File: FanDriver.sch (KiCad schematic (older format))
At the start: 0 parts

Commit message: updated fan control seyion
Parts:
- added Q?: MOSFET_N, symbol MOSFET_N
- added R?: R, symbol R
- added RV?: POT, symbol POT
- added U?: LM324, symbol LM324
- added U?: ADC0832, symbol ADC0832
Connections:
- net labels added: +12V, -12V, GND
- wire segments 0 -> 17
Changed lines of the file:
@@
-EESchema Schematic File Version 2  date Wed 05 Feb 2014 12:50:12 AM EST
+EESchema Schematic File Version 2  date Thu 06 Feb 2014 12:03:54 AM EST
 LIBS:power
 LIBS:device
@@
 Sheet 4 8
 Title ""
-Date "5 feb 2014"
+Date "6 feb 2014"
 Rev ""
 Comp ""
@@
 Comment4 ""
 $EndDescr
-Text HLabel 3300 1900 0    60   Input ~ 0
+$Comp
+L ADC0832 U?
+U 1 1 52F316A2
+P 3550 2150
+F 0 "U?" H 3550 2250 70  0000 C CNN
+F 1 "ADC0832" H 3550 2051 70  0000 C CNN
+	1    3550 2150
+	1    0    0    -1
+$EndComp
+Wire Wire Line
+	5100 3000 5100 3450
+Wire Wire Line
+	5100 2300 6650 2300
+Wire Wire Line
+	7050 1750 7050 2000
+Connection ~ 8400 2900
+Wire Wire Line
+	8400 2900 6400 2900
+Wire Wire Line
+	6400 2900 6400 2500
+Wire Wire Line
+	6400 2500 6650 2500
+Wire Wire Line
+	8400 1800 8400 2200
+Wire Wire Line
+	7650 2400 8100 2400
+Wire Wire Line
+	8400 2600 8400 2950
+Wire Wire Line
+	8400 2950 10850 2950
+Wire Wire Line
+	10850 3150 8450 3150
+Wire Wire Line
+	8450 3150 8450 3450
+Wire Wire Line
+	7050 2800 7050 2850
+Wire Wire Line
+	7050 2850 7300 2850
+Wire Wire Line
+	7300 2850 7300 2800
+Wire Wire Line
+	5100 1450 5100 1650
+Wire Wire Line
+	5100 2500 5100 2150
+Connection ~ 5100 2300
+$Comp
+L GND #PWR?
+U 1 1 52F31662
+P 5100 3450
+F 0 "#PWR?" H 5100 3450 30  0001 C CNN
+F 1 "GND" H 5100 3380 30  0001 C CNN
+	1    5100 3450
+	1    0    0    -1
+$EndComp
+$Comp
+L R R?
+U 1 1 52F31643
+P 5100 1900
+F 0 "R?" V 5180 1900 50  0000 C CNN
+F 1 "R" V 5100 1900 50  0000 C CNN
+	1    5100 1900
+	1    0    0    -1
+$EndComp
+$Comp
+L POT RV?
+U 1 1 52F315F5
+P 5100 2750
+F 0 "RV?" H 5100 2650 50  0000 C CNN
+F 1 "POT" H 5100 2750 50  0000 C CNN
+	1    5100 2750
+	0    -1   1    0
+$EndComp
+$Comp
+L +12V #PWR?
+U 1 1 52F315D4
+P 5100 1450
+F 0 "#PWR?" H 5100 1400 20  0001 C CNN
+F 1 "+12V" H 5100 1550 30  0000 C CNN
+	1    5100 1450
+	1    0    0    -1
+$EndComp
+$Comp
+L -12V #PWR?
+U 1 1 52F31549
+P 7300 2800
+F 0 "#PWR?" H 7300 2930 20  0001 C CNN
+F 1 "-12V" H 7300 2900 30  0000 C CNN
+	1    7300 2800
+	1    0    0    -1
+$EndComp
+$Comp
+L +12V #PWR?
+U 1 1 52F31538
+P 7050 1750
+F 0 "#PWR?" H 7050 1700 20  0001 C CNN
+F 1 "+12V" H 7050 1850 30  0000 C CNN
+	1    7050 1750
+	1    0    0    -1
+$EndComp
+$Comp
+L GND #PWR?
+U 1 1 52F313E3
+P 8450 3450
+F 0 "#PWR?" H 8450 3450 30  0001 C CNN
+F 1 "GND" H 8450 3380 30  0001 C CNN
+	1    8450 3450
+	1    0    0    -1
+$EndComp
+$Comp
+L +12V #PWR?
+U 1 1 52F31370
+P 8400 1800
+F 0 "#PWR?" H 8400 1750 20  0001 C CNN
+F 1 "+12V" H 8400 1900 30  0000 C CNN
+	1    8400 1800
+	1    0    0    -1
+$EndComp
+$Comp
+L MOSFET_N Q?
+U 1 1 52F31276
+P 8300 2400
+F 0 "Q?" H 8310 2570 60  0000 R CNN
+F 1 "MOSFET_N" H 8310 2250 60  0000 R CNN
+	1    8300 2400
+	1    0    0    -1
+$EndComp
+$Comp
+L LM324 U?
+U 1 1 52F311E8
+P 7150 2400
+F 0 "U?" H 7200 2600 60  0000 C CNN
+F 1 "LM324" H 7300 2200 50  0000 C CNN
+	1    7150 2400
+	1    0    0    -1
+$EndComp
+Text HLabel 1650 2400 0    60   Input ~ 0
 FanIn
-Text HLabel 3300 1750 0    60   Output ~ 0
+Text HLabel 1650 2250 0    60   Output ~ 0
 TacOut
-Text HLabel 8250 2750 0    60   Input ~ 0
+Text HLabel 10850 3450 0    60   Input ~ 0
 TacIn
-Text HLabel 8250 2450 0    60   Input ~ 0
+Text HLabel 10850 3150 0    60   Input ~ 0
 PWR-
-Text HLabel 8250 2250 0    60   Output ~ 0
+Text HLabel 10850 2950 0    60   Output ~ 0
 PWR+
 $EndSCHEMATC

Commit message: Updated with correct DAC and ADC for thermo and fan
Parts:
- removed U?: ADC0832, symbol ADC0832
- added R? (x4): R, symbol R
- added U?: MCP4921-E/SN, SO8, symbol MCP4921-E/SN
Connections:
- net labels added: CS_N, CurrentMeasure, MISO, MOSI, S_CLK
- wire segments 17 -> 30
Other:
- moved on the sheet: RV?
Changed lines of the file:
@@
-EESchema Schematic File Version 2  date Thu 06 Feb 2014 12:03:54 AM EST
+EESchema Schematic File Version 2
 LIBS:power
 LIBS:device
@@
 LIBS:valves
 LIBS:InitialKiCadProject-cache
-EELAYER 25  0
+EELAYER 27 0
 EELAYER END
-$Descr A4 11700 8267
+$Descr A4 11693 8268
 encoding utf-8
 Sheet 4 8
 Title ""
-Date "6 feb 2014"
+Date "7 feb 2014"
 Rev ""
 Comp ""
@@
 $EndDescr
 $Comp
-L ADC0832 U?
-U 1 1 52F316A2
-P 3550 2150
-F 0 "U?" H 3550 2250 70  0000 C CNN
-F 1 "ADC0832" H 3550 2051 70  0000 C CNN
-	1    3550 2150
-	1    0    0    -1
-$EndComp
-Wire Wire Line
-	5100 3000 5100 3450
-Wire Wire Line
-	5100 2300 6650 2300
-Wire Wire Line
-	7050 1750 7050 2000
-Connection ~ 8400 2900
-Wire Wire Line
-	8400 2900 6400 2900
-Wire Wire Line
-	6400 2900 6400 2500
-Wire Wire Line
-	6400 2500 6650 2500
-Wire Wire Line
-	8400 1800 8400 2200
-Wire Wire Line
-	7650 2400 8100 2400
-Wire Wire Line
-	8400 2600 8400 2950
-Wire Wire Line
-	8400 2950 10850 2950
-Wire Wire Line
-	10850 3150 8450 3150
-Wire Wire Line
-	8450 3150 8450 3450
-Wire Wire Line
-	7050 2800 7050 2850
-Wire Wire Line
-	7050 2850 7300 2850
-Wire Wire Line
-	7300 2850 7300 2800
-Wire Wire Line
-	5100 1450 5100 1650
-Wire Wire Line
-	5100 2500 5100 2150
-Connection ~ 5100 2300
-$Comp
 L GND #PWR?
 U 1 1 52F31662
-P 5100 3450
-F 0 "#PWR?" H 5100 3450 30  0001 C CNN
-F 1 "GND" H 5100 3380 30  0001 C CNN
-	1    5100 3450
+P 4800 3000
+F 0 "#PWR?" H 4800 3000 30  0001 C CNN
+F 1 "GND" H 4800 2930 30  0001 C CNN
+F 2 "" H 4800 3000 60  0001 C CNN
+F 3 "" H 4800 3000 60  0001 C CNN
+	1    4800 3000
 	1    0    0    -1
 $EndComp
@@
 F 0 "R?" V 5180 1900 50  0000 C CNN
 F 1 "R" V 5100 1900 50  0000 C CNN
+F 2 "" H 5100 1900 60  0001 C CNN
+F 3 "" H 5100 1900 60  0001 C CNN
 	1    5100 1900
 	1    0    0    -1
@@
 L POT RV?
 U 1 1 52F315F5
-P 5100 2750
-F 0 "RV?" H 5100 2650 50  0000 C CNN
-F 1 "POT" H 5100 2750 50  0000 C CNN
-	1    5100 2750
+P 5100 2650
+F 0 "RV?" H 5100 2550 50  0000 C CNN
+F 1 "POT" H 5100 2650 50  0000 C CNN
+F 2 "" H 5100 2650 60  0001 C CNN
+F 3 "" H 5100 2650 60  0001 C CNN
+	1    5100 2650
 	0    -1   1    0
 $EndComp
@@
 F 0 "#PWR?" H 5100 1400 20  0001 C CNN
 F 1 "+12V" H 5100 1550 30  0000 C CNN
+F 2 "" H 5100 1450 60  0001 C CNN
+F 3 "" H 5100 1450 60  0001 C CNN
 	1    5100 1450
 	1    0    0    -1
@@
 F 0 "#PWR?" H 7300 2930 20  0001 C CNN
 F 1 "-12V" H 7300 2900 30  0000 C CNN
+F 2 "" H 7300 2800 60  0001 C CNN
+F 3 "" H 7300 2800 60  0001 C CNN
 	1    7300 2800
 	1    0    0    -1
@@
 F 0 "#PWR?" H 7050 1700 20  0001 C CNN
 F 1 "+12V" H 7050 1850 30  0000 C CNN
+F 2 "" H 7050 1750 60  0001 C CNN
+F 3 "" H 7050 1750 60  0001 C CNN
 	1    7050 1750
 	1    0    0    -1
@@
 L GND #PWR?
 U 1 1 52F313E3
-P 8450 3450
-F 0 "#PWR?" H 8450 3450 30  0001 C CNN
-F 1 "GND" H 8450 3380 30  0001 C CNN
-	1    8450 3450
+P 7600 4450
+F 0 "#PWR?" H 7600 4450 30  0001 C CNN
+F 1 "GND" H 7600 4380 30  0001 C CNN
+F 2 "" H 7600 4450 60  0001 C CNN
+F 3 "" H 7600 4450 60  0001 C CNN
+	1    7600 4450
 	1    0    0    -1
 $EndComp
@@
 F 0 "#PWR?" H 8400 1750 20  0001 C CNN
 F 1 "+12V" H 8400 1900 30  0000 C CNN
+F 2 "" H 8400 1800 60  0001 C CNN
+F 3 "" H 8400 1800 60  0001 C CNN
 	1    8400 1800
 	1    0    0    -1
@@
 F 0 "Q?" H 8310 2570 60  0000 R CNN
 F 1 "MOSFET_N" H 8310 2250 60  0000 R CNN
+F 2 "" H 8300 2400 60  0001 C CNN
+F 3 "" H 8300 2400 60  0001 C CNN
 	1    8300 2400
 	1    0    0    -1
@@
 F 0 "U?" H 7200 2600 60  0000 C CNN
 F 1 "LM324" H 7300 2200 50  0000 C CNN
+F 2 "" H 7150 2400 60  0001 C CNN
+F 3 "" H 7150 2400 60  0001 C CNN
 	1    7150 2400
 	1    0    0    -1
 $EndComp
-Text HLabel 1650 2400 0    60   Input ~ 0
+Text HLabel 1950 3200 0    60   Input ~ 0
 FanIn
-Text HLabel 1650 2250 0    60   Output ~ 0
+Text HLabel 1650 5050 0    60   Output ~ 0
 TacOut
-Text HLabel 10850 3450 0    60   Input ~ 0
+Text HLabel 10700 5050 0    60   Input ~ 0
 TacIn
-Text HLabel 10850 3150 0    60   Input ~ 0
+Text HLabel 10900 3300 0    60   Input ~ 0
 PWR-
 Text HLabel 10850 2950 0    60   Output ~ 0
 PWR+
+Text HLabel 1950 3300 0    60   Output ~ 0
+CurrentMeasure
+$Comp
+L R R?
+U 1 1 52F43F3A
+P 7600 4000
+F 0 "R?" V 7680 4000 50  0000 C CNN
+F 1 "R" V 7600 4000 50  0000 C CNN
+F 2 "" H 7600 4000 60  0001 C CNN
+F 3 "" H 7600 4000 60  0001 C CNN
+	1    7600 4000
+	1    0    0    -1
+$EndComp
+Connection ~ 7600 3300
+Wire Wire Line
+	7600 4250 7600 4450
+Wire Wire Line
+	6600 2500 6650 2500
+Wire Wire Line
+	6600 3300 6600 2500
+Wire Wire Line
+	1950 3300 10900 3300
+Wire Wire Line
+	7600 3750 7600 3300
+Wire Wire Line
+	10700 5050 1650 5050
+Connection ~ 5100 2300
+Wire Wire Line
+	5100 2150 5100 2400
+Wire Wire Line
+	5100 1450 5100 1650
+Wire Wire Line
+	7300 2850 7300 2800
+Wire Wire Line
+	7050 2850 7300 2850
+Wire Wire Line
+	7050 2800 7050 2850
+Wire Wire Line
+	8400 2950 10850 2950
+Wire Wire Line
+	8400 2600 8400 2950
+Wire Wire Line
+	7650 2400 8100 2400
+Wire Wire Line
+	8400 1800 8400 2200
+Connection ~ 8400 2900
+Wire Wire Line
+	7050 1750 7050 2000
+Wire Wire Line
+	5100 2300 6650 2300
+Connection ~ 6600 3300
+$Comp
+L R R?
+U 1 1 52F4401D
+P 4300 2200
+F 0 "R?" V 4380 2200 50  0000 C CNN
+F 1 "R" V 4300 2200 50  0000 C CNN
+F 2 "" H 4300 2200 60  0001 C CNN
+F 3 "" H 4300 2200 60  0001 C CNN
+	1    4300 2200
+	0    -1   -1   0
+$EndComp
+Wire Wire Line
+	3700 2200 4050 2200
+Wire Wire Line
+	4550 2200 5100 2200
+Connection ~ 5100 2200
+$Comp
+L R R?
+U 1 1 52F44054
+P 6000 2850
+F 0 "R?" V 6080 2850 50  0000 C CNN
+F 1 "R" V 6000 2850 50  0000 C CNN
+F 2 "" H 6000 2850 60  0001 C CNN
+F 3 "" H 6000 2850 60  0001 C CNN
+	1    6000 2850
+	1    0    0    -1
+$EndComp
+Wire Wire Line
+	6000 2600 6000 2300
+Connection ~ 6000 2300
+Wire Wire Line
+	6000 3100 6000 3200
+Wire Wire Line
+	6000 3200 1950 3200
+Text HLabel 2050 1800 0    60   Output ~ 0
+MISO
+Text HLabel 2100 2050 0    60   Input ~ 0
+MOSI
+Text HLabel 2100 2250 0    60   Input ~ 0
+CS_N
+Text HLabel 2100 2150 0    60   Input ~ 0
+S_CLK
+$Comp
+L MCP4921-E/SN U?
+U 1 1 52F441DE
+P 3150 2200
+F 0 "U?" H 3150 2550 40  0000 L BNN
+F 1 "MCP4921-E/SN" H 3150 2500 40  0000 L BNN
+F 2 "SO8" H 3150 2200 30  0000 C CIN
+F 3 "" H 3150 2200 60  0000 C CNN
+	1    3150 2200
+	1    0    0    -1
+$EndComp
+Wire Wire Line
+	2100 2050 2600 2050
+Wire Wire Line
+	2100 2150 2600 2150
+Wire Wire Line
+	2100 2250 2600 2250
+$Comp
+L R R?
+U 1 1 52F44272
+P 2350 2750
+F 0 "R?" V 2430 2750 50  0000 C CNN
+F 1 "R" V 2350 2750 50  0000 C CNN
+F 2 "" H 2350 2750 60  0001 C CNN
+F 3 "" H 2350 2750 60  0001 C CNN
+	1    2350 2750
+	1    0    0    -1
+$EndComp
+Wire Wire Line
+	2350 2500 2350 2350
+Wire Wire Line
+	2350 2350 2600 2350
+Wire Wire Line
+	2350 3000 2350 3200
+Connection ~ 2350 3200
+Wire Wire Line
+	4950 2650 4800 2650
+Wire Wire Line
+	4800 2650 4800 3000
 $EndSCHEMATC

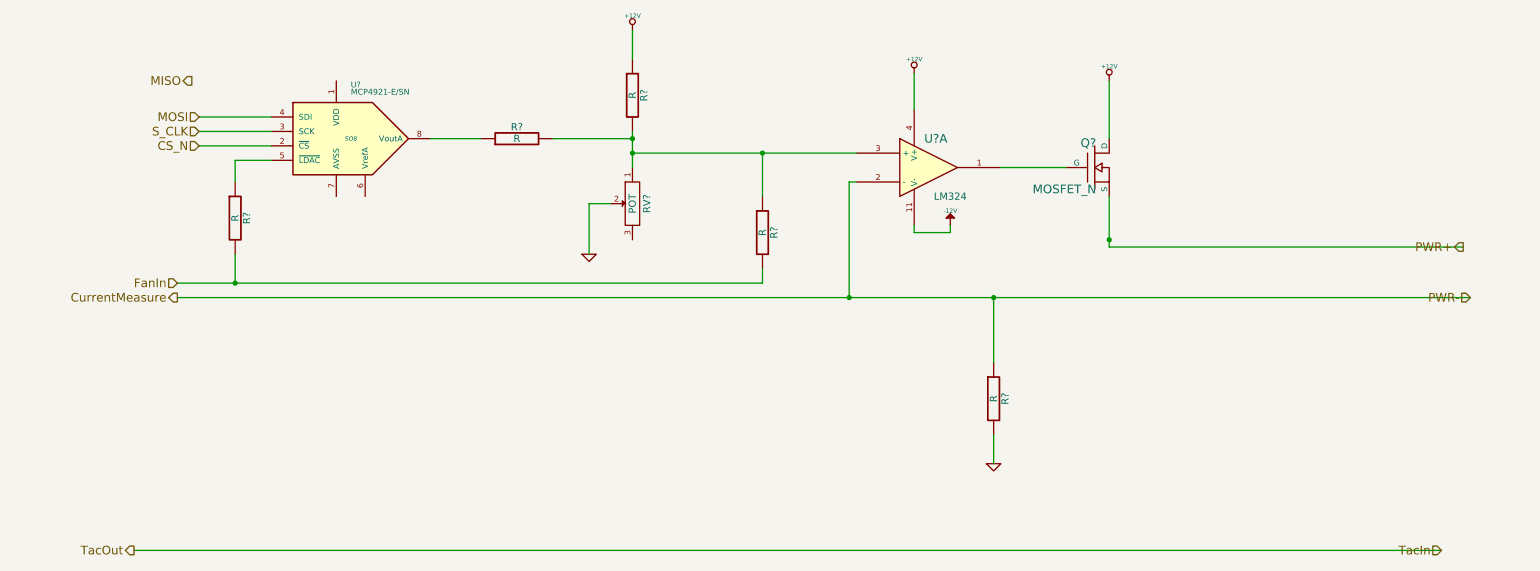
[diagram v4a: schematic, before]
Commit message: Added Relay Driver
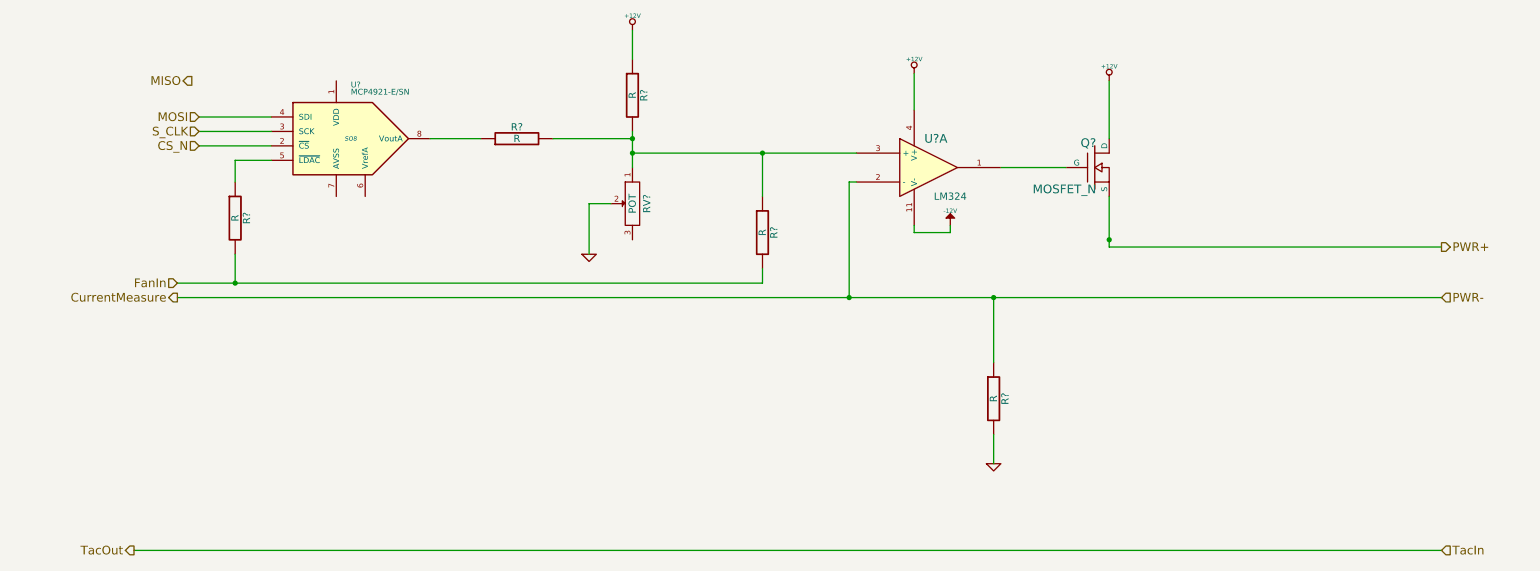
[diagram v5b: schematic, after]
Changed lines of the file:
@@
 LIBS:contrib
 LIBS:valves
+LIBS:arduino_shieldsNCL
+LIBS:spdt
 LIBS:InitialKiCadProject-cache
 EELAYER 27 0
@@
 Text HLabel 1650 5050 0    60   Output ~ 0
 TacOut
-Text HLabel 10700 5050 0    60   Input ~ 0
+Text HLabel 10700 5050 2    60   Input ~ 0
 TacIn
-Text HLabel 10900 3300 0    60   Input ~ 0
+Text HLabel 10700 3300 2    60   Input ~ 0
 PWR-
-Text HLabel 10850 2950 0    60   Output ~ 0
+Text HLabel 10700 2950 2    60   Output ~ 0
 PWR+
 Text HLabel 1950 3300 0    60   Output ~ 0
@@
 	6600 3300 6600 2500
 Wire Wire Line
-	1950 3300 10900 3300
+	1950 3300 6600 3300
+Wire Wire Line
+	6600 3300 7600 3300
+Wire Wire Line
+	7600 3300 10700 3300
 Wire Wire Line
 	7600 3750 7600 3300
@@
 Connection ~ 5100 2300
 Wire Wire Line
-	5100 2150 5100 2400
+	5100 2150 5100 2200
+Wire Wire Line
+	5100 2200 5100 2300
+Wire Wire Line
+	5100 2300 5100 2400
 Wire Wire Line
 	5100 1450 5100 1650
@@
 	7050 2800 7050 2850
 Wire Wire Line
-	8400 2950 10850 2950
-Wire Wire Line
-	8400 2600 8400 2950
+	8400 2950 10700 2950
+Wire Wire Line
+	8400 2600 8400 2900
+Wire Wire Line
+	8400 2900 8400 2950
 Wire Wire Line
 	7650 2400 8100 2400
@@
 	7050 1750 7050 2000
 Wire Wire Line
-	5100 2300 6650 2300
+	5100 2300 6000 2300
+Wire Wire Line
+	6000 2300 6650 2300
 Connection ~ 6600 3300
 $Comp
@@
 	6000 3100 6000 3200
 Wire Wire Line
-	6000 3200 1950 3200
+	6000 3200 2350 3200
+Wire Wire Line
+	2350 3200 1950 3200
 Text HLabel 2050 1800 0    60   Output ~ 0
 MISO

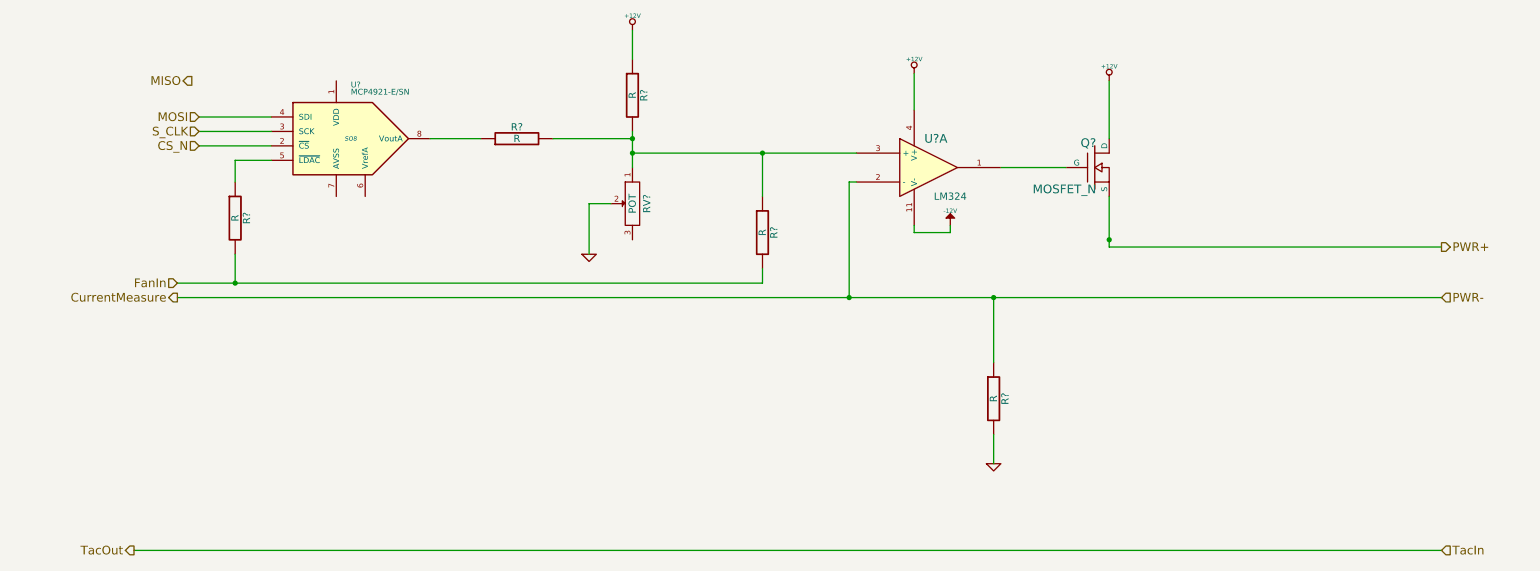
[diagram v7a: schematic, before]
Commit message: WIRED BLOCK DIAGRAM TOGETHER AND ADDED ARDUINO BLOCK
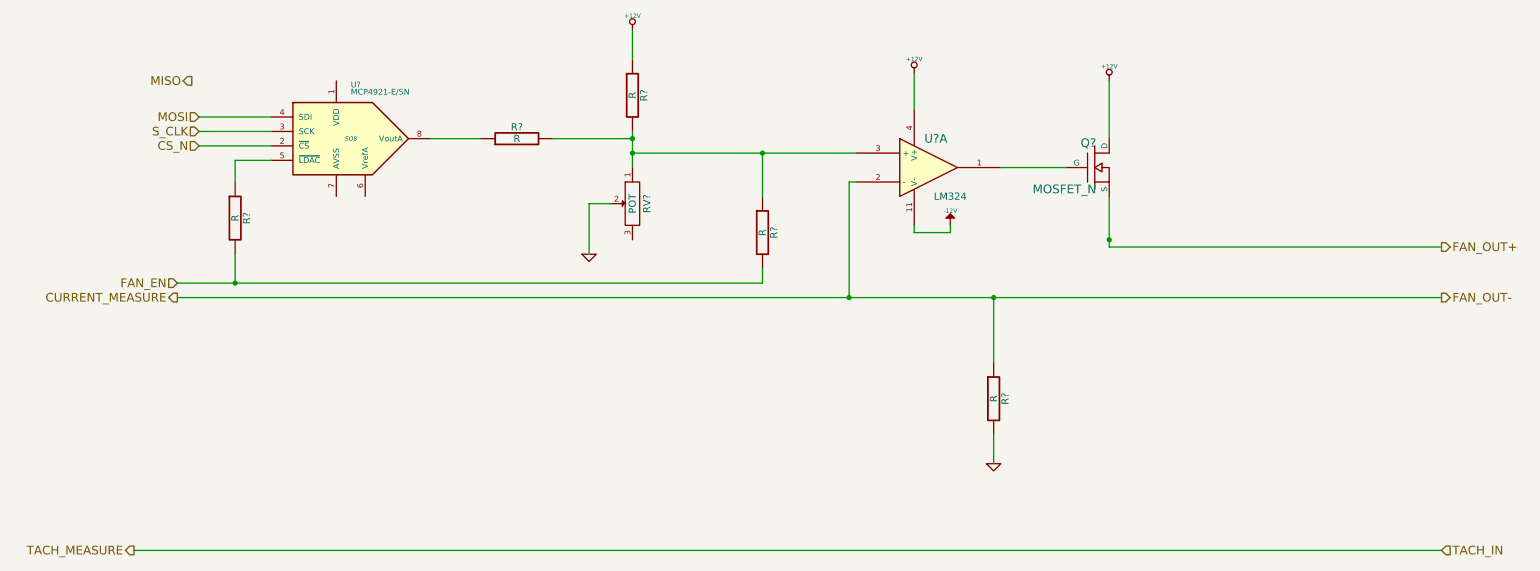
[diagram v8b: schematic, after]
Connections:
- net CurrentMeasure renamed CURRENT_MEASURE
- net FanIn renamed FAN_EN
- net PWR+ renamed FAN_OUT+
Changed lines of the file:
@@
-EESchema Schematic File Version 2  date Sat 08 Feb 2014 08:25:16 PM EST
+EESchema Schematic File Version 2  date Sat 08 Feb 2014 11:37:49 PM EST
 LIBS:power
 LIBS:device
@@
 $EndComp
 Text HLabel 1950 3200 0    60   Input ~ 0
-FanIn
+FAN_EN
 Text HLabel 1650 5050 0    60   Output ~ 0
-TacOut
+TACH_MEASURE
 Text HLabel 10700 5050 2    60   Input ~ 0
-TacIn
-Text HLabel 10700 3300 2    60   Input ~ 0
-PWR-
+TACH_IN
+Text HLabel 10700 3300 2    60   Output ~ 0
+FAN_OUT-
 Text HLabel 10700 2950 2    60   Output ~ 0
-PWR+
+FAN_OUT+
 Text HLabel 1950 3300 0    60   Output ~ 0
-CurrentMeasure
+CURRENT_MEASURE
 $Comp
 L R R?
